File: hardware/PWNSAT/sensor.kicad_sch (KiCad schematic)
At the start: 1 part, among them J3 Sensors

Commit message: feat(Hw):PCB_PwnSat_And_Battery_Updated
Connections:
- net R0_MISO: now also J3.9 (Pin_9); no longer J3.7 (Pin_7)
- net R0_MOSI: now also J3.7 (Pin_7); no longer J3.9 (Pin_9)
- net R1_BUSY: now also J3.35 (Pin_35); no longer J3.37 (Pin_37)
- net R1_RST: now also J3.37 (Pin_37); no longer J3.35 (Pin_35)
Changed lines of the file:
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@@
 	(hierarchical_label "R1_BUSY"
 		(shape input)
-		(at 69.85 83.82 180)
+		(at 69.85 81.28 180)
 		(effects
 			(font
@@
 	(hierarchical_label "R0_MOSI"
 		(shape input)
+		(at 69.85 45.72 180)
+		(effects
+			(font
+				(size 1.27 1.27)
+			)
+			(justify right)
+		)
+	)
+	(hierarchical_label "R0_DIO3"
+		(shape input)
+		(at 69.85 55.88 180)
+		(effects
+			(font
+				(size 1.27 1.27)
+			)
+			(justify right)
+		)
+	)
+	(hierarchical_label "R0_ANT_SW"
+		(shape input)
+		(at 69.85 63.5 180)
+		(effects
+			(font
+				(size 1.27 1.27)
+			)
+			(justify right)
+		)
+	)
+	(hierarchical_label "R1_NSS"
+		(shape input)
+		(at 69.85 71.12 180)
+		(effects
+			(font
+				(size 1.27 1.27)
+			)
+			(justify right)
+		)
+	)
+	(hierarchical_label "R1_MOSI"
+		(shape input)
+		(at 69.85 78.74 180)
+		(effects
+			(font
+				(size 1.27 1.27)
+			)
+			(justify right)
+		)
+	)
+	(hierarchical_label "R0_SCK"
+		(shape input)
+		(at 69.85 43.18 180)
+		(effects
+			(font
+				(size 1.27 1.27)
+			)
+			(justify right)
+		)
+	)
+	(hierarchical_label "R0_MISO"
+		(shape input)
 		(at 69.85 48.26 180)
-		(effects
-			(font
-				(size 1.27 1.27)
-			)
-			(justify right)
-		)
-	)
-	(hierarchical_label "R0_DIO3"
-		(shape input)
-		(at 69.85 55.88 180)
-		(effects
-			(font
-				(size 1.27 1.27)
-			)
-			(justify right)
-		)
-	)
-	(hierarchical_label "R0_ANT_SW"
-		(shape input)
-		(at 69.85 63.5 180)
-		(effects
-			(font
-				(size 1.27 1.27)
-			)
-			(justify right)
-		)
-	)
-	(hierarchical_label "R1_NSS"
-		(shape input)
-		(at 69.85 71.12 180)
-		(effects
-			(font
-				(size 1.27 1.27)
-			)
-			(justify right)
-		)
-	)
-	(hierarchical_label "R1_MOSI"
-		(shape input)
-		(at 69.85 78.74 180)
-		(effects
-			(font
-				(size 1.27 1.27)
-			)
-			(justify right)
-		)
-	)
-	(hierarchical_label "R0_SCK"
-		(shape input)
-		(at 69.85 43.18 180)
-		(effects
-			(font
-				(size 1.27 1.27)
-			)
-			(justify right)
-		)
-	)
-	(hierarchical_label "R0_MISO"
-		(shape input)
-		(at 69.85 45.72 180)
 		(effects
 			(font
@@
 	(hierarchical_label "R1_RST"
 		(shape input)
-		(at 69.85 81.28 180)
-		(effects
-			(font
+		(at 69.85 83.82 180)
+		(effects
+			(font

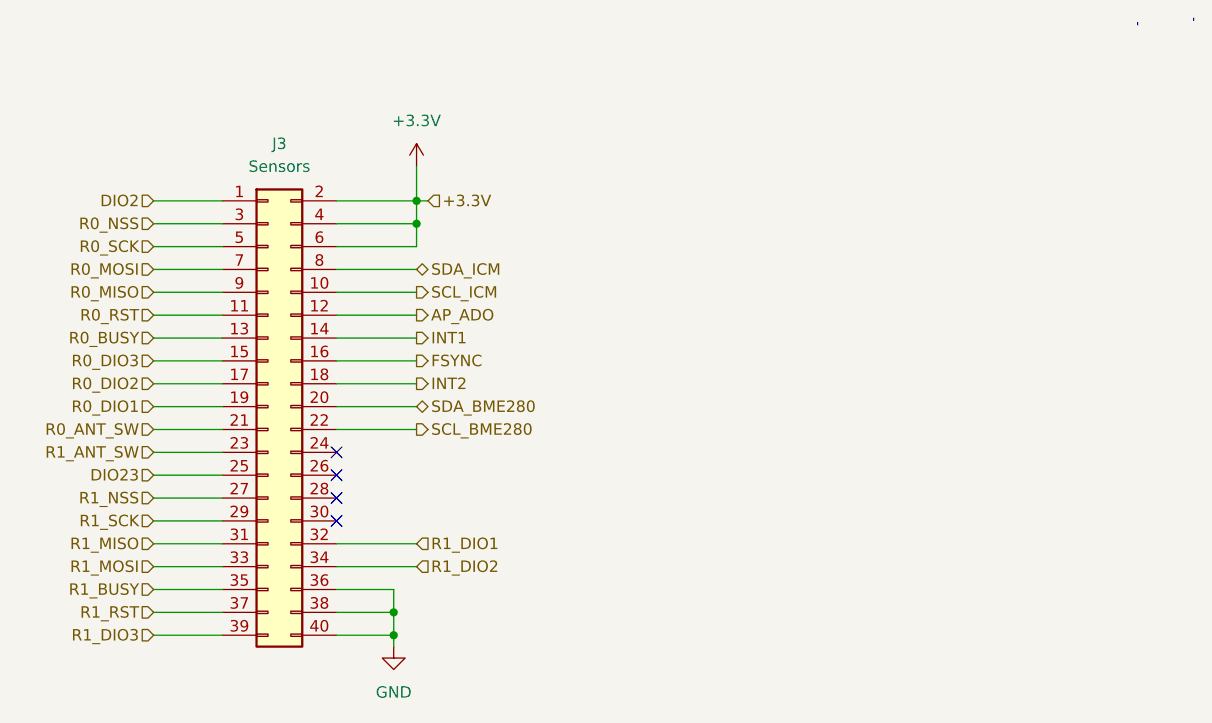
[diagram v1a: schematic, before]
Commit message: feat(Hw):Route_Updating_PWNCube_Board
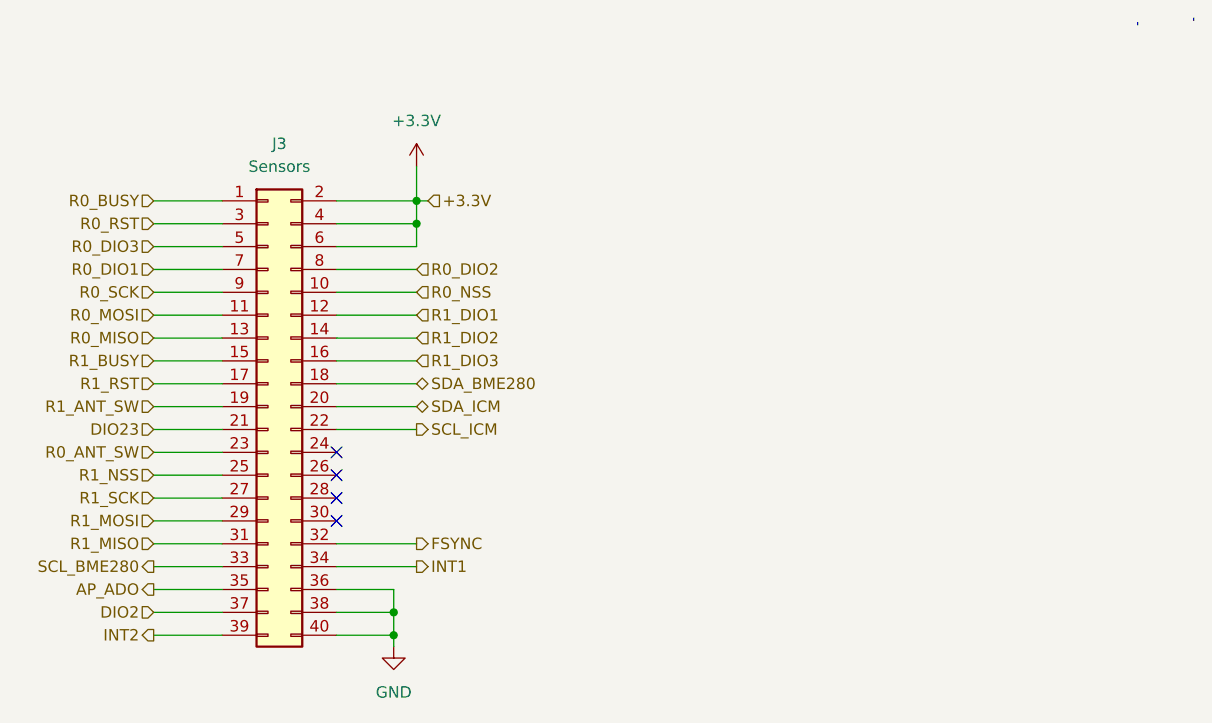
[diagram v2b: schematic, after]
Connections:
- net AP_ADO: now also J3.35 (Pin_35); no longer J3.12 (Pin_12)
- net DIO2: now also J3.37 (Pin_37); no longer J3.1 (Pin_1)
- net DIO23: now also J3.21 (Pin_21); no longer J3.25 (Pin_25)
- net FSYNC: now also J3.32 (Pin_32); no longer J3.16 (Pin_16)
- net INT1: now also J3.34 (Pin_34); no longer J3.14 (Pin_14)
- net INT2: now also J3.39 (Pin_39); no longer J3.18 (Pin_18)
- net R0_ANT_SW: now also J3.23 (Pin_23); no longer J3.21 (Pin_21)
- net R0_BUSY: now also J3.1 (Pin_1); no longer J3.13 (Pin_13)
- net R0_DIO1: now also J3.7 (Pin_7); no longer J3.19 (Pin_19)
- net R0_DIO2: now also J3.8 (Pin_8); no longer J3.17 (Pin_17)
- net R0_DIO3: now also J3.5 (Pin_5); no longer J3.15 (Pin_15)
- net R0_MISO: now also J3.13 (Pin_13); no longer J3.9 (Pin_9)
- net R0_MOSI: now also J3.11 (Pin_11); no longer J3.7 (Pin_7)
- net R0_NSS: now also J3.10 (Pin_10); no longer J3.3 (Pin_3)
- net R0_RST: now also J3.3 (Pin_3); no longer J3.11 (Pin_11)
- net R0_SCK: now also J3.9 (Pin_9); no longer J3.5 (Pin_5)
- net R1_ANT_SW: now also J3.19 (Pin_19); no longer J3.23 (Pin_23)
- net R1_BUSY: now also J3.15 (Pin_15); no longer J3.35 (Pin_35)
- net R1_DIO1: now also J3.12 (Pin_12); no longer J3.32 (Pin_32)
- net R1_DIO2: now also J3.14 (Pin_14); no longer J3.34 (Pin_34)
- net R1_DIO3: now also J3.16 (Pin_16); no longer J3.39 (Pin_39)
- net R1_MOSI: now also J3.29 (Pin_29); no longer J3.33 (Pin_33)
- net R1_NSS: now also J3.25 (Pin_25); no longer J3.27 (Pin_27)
- net R1_RST: now also J3.17 (Pin_17); no longer J3.37 (Pin_37)
- net R1_SCK: now also J3.27 (Pin_27); no longer J3.29 (Pin_29)
- net SCL_BME280: now also J3.33 (Pin_33); no longer J3.22 (Pin_22)
- net SCL_ICM: now also J3.22 (Pin_22); no longer J3.10 (Pin_10)
- net SDA_BME280: now also J3.18 (Pin_18); no longer J3.20 (Pin_20)
- net SDA_ICM: now also J3.20 (Pin_20); no longer J3.8 (Pin_8)
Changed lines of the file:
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@@
 	(hierarchical_label "R0_DIO1"
 		(shape input)
+		(at 69.85 45.72 180)
+		(effects
+			(font
+				(size 1.27 1.27)
+			)
+			(justify right)
+		)
+	)
+	(hierarchical_label "R0_BUSY"
+		(shape input)
+		(at 69.85 38.1 180)
+		(effects
+			(font
+				(size 1.27 1.27)
+			)
+			(justify right)
+		)
+	)
+	(hierarchical_label "R1_ANT_SW"
+		(shape input)
 		(at 69.85 60.96 180)
 		(effects
@@
 		)
 	)
-	(hierarchical_label "R0_BUSY"
-		(shape input)
-		(at 69.85 53.34 180)
-		(effects
-			(font
-				(size 1.27 1.27)
-			)
-			(justify right)
-		)
-	)
-	(hierarchical_label "R1_ANT_SW"
-		(shape input)
-		(at 69.85 66.04 180)
-		(effects
-			(font
-				(size 1.27 1.27)
-			)
-			(justify right)
-		)
-	)
 	(hierarchical_label "R1_BUSY"
 		(shape input)
-		(at 69.85 81.28 180)
+		(at 69.85 55.88 180)
 		(effects
 			(font
@@
 	(hierarchical_label "R1_DIO2"
 		(shape input)
-		(at 99.06 78.74 0)
+		(at 99.06 53.34 0)
 		(effects
 			(font
@@
 	(hierarchical_label "SDA_BME280"
 		(shape bidirectional)
-		(at 99.06 60.96 0)
+		(at 99.06 58.42 0)
 		(effects
 			(font
@@
 	(hierarchical_label "FSYNC"
 		(shape output)
-		(at 99.06 55.88 0)
+		(at 99.06 76.2 0)
 		(effects
 			(font
@@
 	(hierarchical_label "R1_SCK"
 		(shape input)
+		(at 69.85 71.12 180)
+		(effects
+			(font
+				(size 1.27 1.27)
+			)
+			(justify right)
+		)
+	)
+	(hierarchical_label "R1_MISO"
+		(shape input)
+		(at 69.85 76.2 180)
+		(effects
+			(font
+				(size 1.27 1.27)
+			)
+			(justify right)
+		)
+	)
+	(hierarchical_label "R0_NSS"
+		(shape input)
+		(at 99.06 48.26 0)
+		(effects
+			(font
+				(size 1.27 1.27)
+			)
+			(justify left)
+		)
+	)
+	(hierarchical_label "DIO2"
+		(shape input)
+		(at 69.85 83.82 180)
+		(effects
+			(font
+				(size 1.27 1.27)
+			)
+			(justify right)
+		)
+	)
+	(hierarchical_label "INT2"
+		(shape output)
+		(at 69.85 86.36 180)
+		(effects
+			(font
+				(size 1.27 1.27)
+			)
+			(justify right)
+		)
+	)
+	(hierarchical_label "R0_MOSI"
+		(shape input)
+		(at 69.85 50.8 180)
+		(effects
+			(font
+				(size 1.27 1.27)
+			)
+			(justify right)
+		)
+	)
+	(hierarchical_label "R0_DIO3"
+		(shape input)
+		(at 69.85 43.18 180)
+		(effects
+			(font
+				(size 1.27 1.27)
+			)
+			(justify right)
+		)
+	)
+	(hierarchical_label "R0_ANT_SW"
+		(shape input)
+		(at 69.85 66.04 180)
+		(effects
+			(font
+				(size 1.27 1.27)
+			)
+			(justify right)
+		)
+	)
+	(hierarchical_label "R1_NSS"
+		(shape input)
+		(at 69.85 68.58 180)
+		(effects
+			(font
+				(size 1.27 1.27)
+			)
+			(justify right)
+		)
+	)
+	(hierarchical_label "R1_MOSI"
+		(shape input)
 		(at 69.85 73.66 180)
 		(effects
@@
 		)
 	)
-	(hierarchical_label "R1_MISO"
-		(shape input)
-		(at 69.85 76.2 180)
-		(effects
-			(font
-				(size 1.27 1.27)
-			)
-			(justify right)
-		)
-	)
-	(hierarchical_label "R0_NSS"
-		(shape input)
-		(at 69.85 40.64 180)
-		(effects
-			(font
-				(size 1.27 1.27)
-			)
-			(justify right)
-		)
-	)
-	(hierarchical_label "DIO2"
-		(shape input)
-		(at 69.85 38.1 180)
-		(effects
-			(font
-				(size 1.27 1.27)
-			)
-			(justify right)
-		)
-	)
-	(hierarchical_label "INT2"
-		(shape output)
-		(at 99.06 58.42 0)
-		(effects
-			(font
-				(size 1.27 1.27)
-			)
-			(justify left)
-		)
-	)
-	(hierarchical_label "R0_MOSI"
-		(shape input)
-		(at 69.85 45.72 180)
-		(effects
-			(font
-				(size 1.27 1.27)
-			)
-			(justify right)
-		)
-	)
-	(hierarchical_label "R0_DIO3"
-		(shape input)
-		(at 69.85 55.88 180)
-		(effects
-			(font
-				(size 1.27 1.27)
-			)
-			(justify right)
-		)
-	)
-	(hierarchical_label "R0_ANT_SW"
-		(shape input)
-		(at 69.85 63.5 180)
-		(effects
-			(font
-				(size 1.27 1.27)
-			)
-			(justify right)
-		)
-	)
-	(hierarchical_label "R1_NSS"
-		(shape input)
-		(at 69.85 71.12 180)
-		(effects
-			(font
-				(size 1.27 1.27)
-			)
-			(justify right)
-		)
-	)
-	(hierarchical_label "R1_MOSI"
-		(shape input)
-		(at 69.85 78.74 180)
-		(effects
-			(font
-				(size 1.27 1.27)
-			)
-			(justify right)
-		)
-	)
 	(hierarchical_label "R0_SCK"
 		(shape input)
-		(at 69.85 43.18 180)
+		(at 69.85 48.26 180)
 		(effects
 			(font
@@
 	(hierarchical_label "R0_MISO"
 		(shape input)
-		(at 69.85 48.26 180)
+		(at 69.85 53.34 180)
 		(effects
 			(font
@@
 	(hierarchical_label "SCL_ICM"
 		(shape output)
-		(at 99.06 48.26 0)
+		(at 99.06 63.5 0)
 		(effects
 			(font
@@
 	(hierarchical_label "SDA_ICM"
 		(shape bidirectional)
+		(at 99.06 60.96 0)
+		(effects
+			(font
+				(size 1.27 1.27)
+			)
+			(justify left)
+		)
+	)
+	(hierarchical_label "INT1"
+		(shape output)
+		(at 99.06 78.74 0)
+		(effects
+			(font
+				(size 1.27 1.27)
+			)
+			(justify left)
+		)
+	)
+	(hierarchical_label "R1_DIO1"
+		(shape input)
+		(at 99.06 50.8 0)
+		(effects
+			(font
+				(size 1.27 1.27)
+			)
+			(justify left)
+		)
+	)
+	(hierarchical_label "DIO23"
+		(shape input)
+		(at 69.85 63.5 180)
+		(effects
+			(font
+				(size 1.27 1.27)
+			)
+			(justify right)
+		)
+	)
+	(hierarchical_label "R0_RST"
+		(shape input)
+		(at 69.85 40.64 180)
+		(effects
+			(font
+				(size 1.27 1.27)
+			)
+			(justify right)
+		)
+	)
+	(hierarchical_label "R0_DIO2"
+		(shape input)
 		(at 99.06 45.72 0)
 		(effects
@@
 		)
 	)
-	(hierarchical_label "INT1"
-		(shape output)
-		(at 99.06 53.34 0)
-		(effects
-			(font
-				(size 1.27 1.27)
-			)
-			(justify left)
-		)
-	)
-	(hierarchical_label "R1_DIO1"
-		(shape input)
-		(at 99.06 76.2 0)
-		(effects
-			(font
-				(size 1.27 1.27)
-			)
-			(justify left)
-		)
-	)
-	(hierarchical_label "DIO23"
-		(shape input)
-		(at 69.85 68.58 180)
-		(effects
-			(font
-				(size 1.27 1.27)
-			)
-			(justify right)
-		)
-	)
-	(hierarchical_label "R0_RST"
-		(shape input)
-		(at 69.85 50.8 180)
-		(effects
-			(font
-				(size 1.27 1.27)
-			)
-			(justify right)
-		)
-	)
-	(hierarchical_label "R0_DIO2"
+	(hierarchical_label "+3.3V"
+		(shape input)
+		(at 100.33 38.1 0)
+		(effects
+			(font
+				(size 1.27 1.27)
+			)
+			(justify left)
+		)
+	)
+	(hierarchical_label "AP_ADO"
+		(shape output)
+		(at 69.85 81.28 180)
+		(effects
+			(font
+				(size 1.27 1.27)
+			)
+			(justify right)
+		)
+	)
+	(hierarchical_label "SCL_BME280"
+		(shape output)
+		(at 69.85 78.74 180)
+		(effects
+			(font
+				(size 1.27 1.27)
+			)
+			(justify right)
+		)
+	)
+	(hierarchical_label "R1_RST"
 		(shape input)
 		(at 69.85 58.42 180)
@@
 		)
 	)
-	(hierarchical_label "+3.3V"
-		(shape input)
-		(at 100.33 38.1 0)
-		(effects
-			(font
-				(size 1.27 1.27)
-			)
-			(justify left)
-		)
-	)
-	(hierarchical_label "AP_ADO"
-		(shape output)
-		(at 99.06 50.8 0)
-		(effects
-			(font
-				(size 1.27 1.27)
-			)
-			(justify left)
-		)
-	)
-	(hierarchical_label "SCL_BME280"
-		(shape output)
-		(at 99.06 63.5 0)
-		(effects
-			(font
-				(size 1.27 1.27)
-			)
-			(justify left)
-		)
-	)
-	(hierarchical_label "R1_RST"
-		(shape input)
-		(at 69.85 83.82 180)
-		(effects
-			(font
-				(size 1.27 1.27)
-			)
-			(justify right)
-		)
-	)
 	(hierarchical_label "R1_DIO3"
 		(shape input)
-		(at 69.85 86.36 180)
-		(effects
-			(font
-				(size 1.27 1.27)
-			)
-			(justify right)
-		)
-	)
+		(at 99.06 55.88 0)
+		(effects
+			(font
+				(size 1.27 1.27)
+			)
+			(justify left)
+		)
+	)
